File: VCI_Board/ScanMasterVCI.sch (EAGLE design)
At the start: 72 parts, among them IC1 XMEGA16A4A, IC2 CD4081B, IC8 SN74AHCT1G04, Q13 MMBT3904, Q14 MMBT3904, Q15 MMBT3904, Q16 MMBT3904, Q17 MMBT3904, Q2 MMBT4403, Q3 MMBT3904, Q4 MMBT4403, Q7 ZXMP6A17G, U1 MAX17502FATB+, U2 SN65HVDA195-Q1, U3 MAX17502EATB+

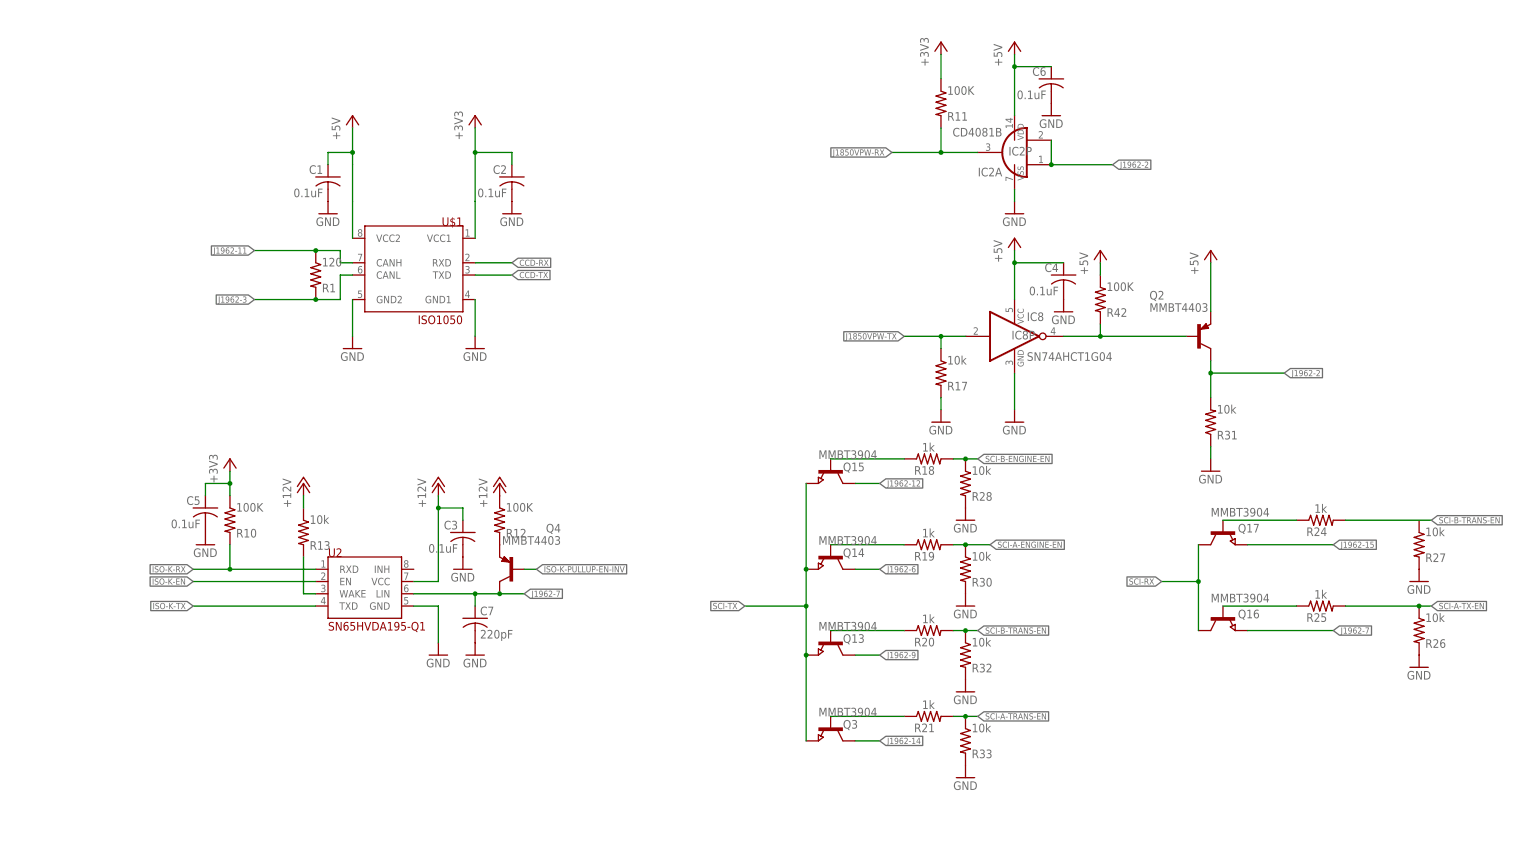
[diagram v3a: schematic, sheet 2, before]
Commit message: Re-wrote ISO9141 pull-up, J1850VPW circuit. ISO9141 pull-up resistor activation works on ISO-K-EN line now, removing the need for ISO-K-PULLUP-EN-INV line. However, it requires a double-transistor to work. J1850VPW circuit now works on +8V like it should, and the RX uses a simple voltage divider to judge the current state of J1850+. Credit goes to Konstantin for his suggestions on the circuits.
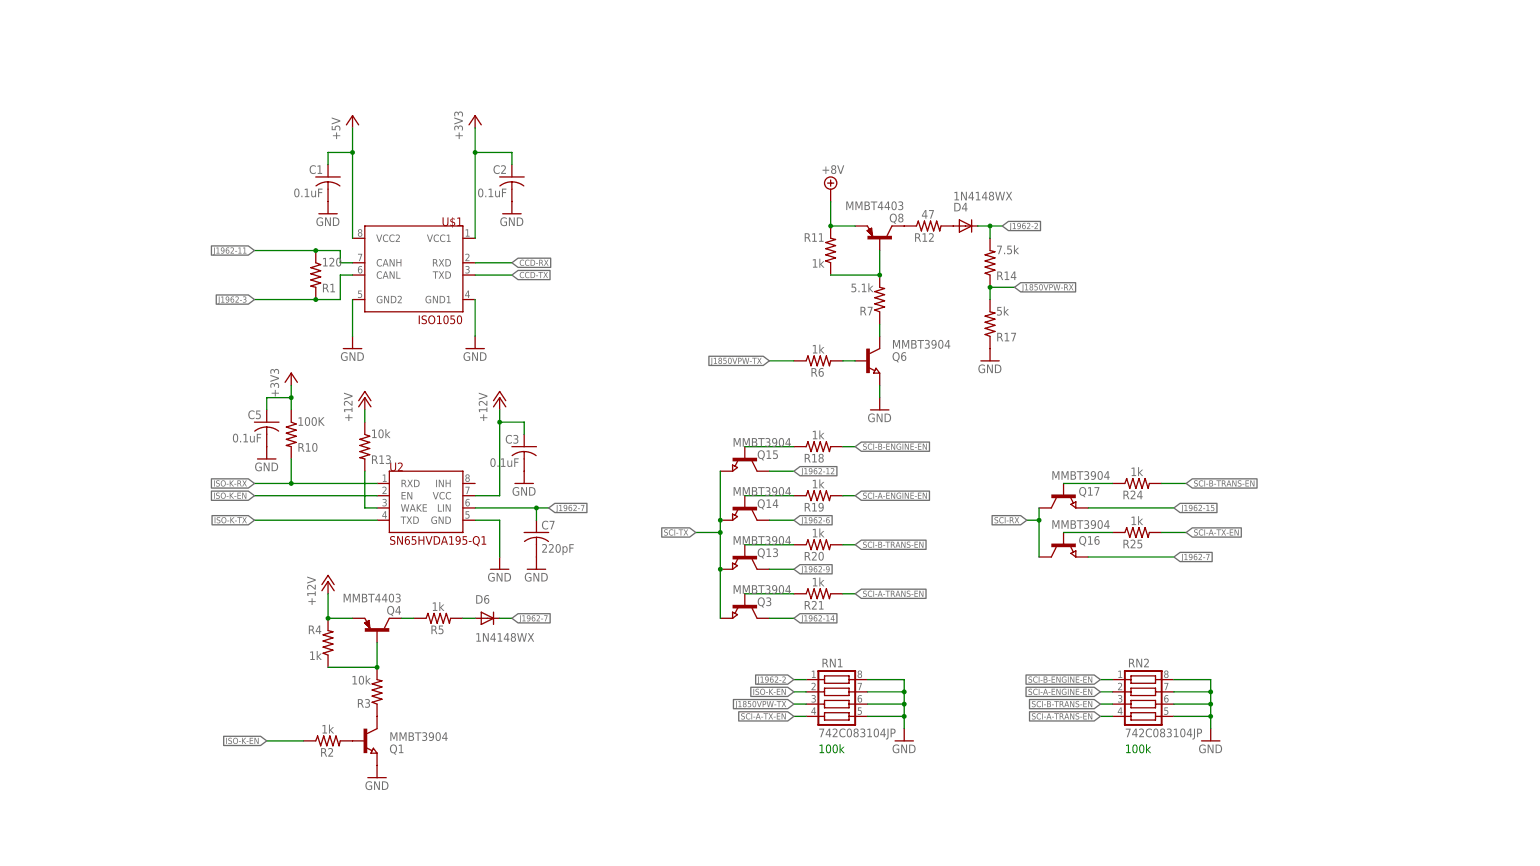
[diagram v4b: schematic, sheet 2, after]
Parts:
- removed C4, C6: 0.1uF, adafruit:C-USC0805
- removed IC2: CD4081B, 40xx:4081D
- removed IC8: SN74AHCT1G04, 74xx-little-us:74AHC1G04DBV
- removed Q2: MMBT4403, transistor-pnp:MMBT4403LT1SMD
- removed R26, R27, R28, R30, R32, R33: 10k, adafruit:R-US_R0805
- removed R31: 10k, adafruit:R-US_R0805W
- removed R42: 100K, adafruit:R-US_R0805W
- added D4, D6: 1N4148WX, diode:DIODE-SOD323-R
- added Q1, Q6: MMBT3904, semicon-smd-ipc:NPN-TRANSISTOR_SOT23
- added Q5: ZXTR2108FQ, customics:ZXTR2108FQ
- added Q8: MMBT4403, transistor-pnp:MMBT4403LT1SMD
- added R14: 7.5k, adafruit:R-US_R0805
- added R2, R4, R5, R6: 1k, adafruit:R-US_R0805
- added R3: 10k, adafruit:R-US_R0805
- added R7: 5.1k, adafruit:R-US_R0805
- added RN1, RN2: 742C083104JP, resistor-net:CTS742C083
- R11: value 100K -> 1k; device adafruit:R-US_R0805W -> adafruit:R-US_R0805
- R12: value 100K -> 47; device adafruit:R-US_R0805W -> adafruit:R-US_R0805
- R17: value 10k -> 5k
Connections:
- removed net ISO-K-PULLUP-EN-INV: IC1.PD4, Q4.B
- removed net J1962-5: J1962_1.5
- removed net N$1: U$1.VCC2
- removed net N$4: U$1.VCC1
- removed net N$5: IC8A.O, Q2.B, R42.2
- new net +8V: Q5.+8V, Q8.E, R11.2
- new net N$11: Q4.B, R3.2, R4.1
- new net N$26: Q6.C, R7.1
- new net N$27: Q4.C, R5.1
- new net N$28: Q8.B, R11.1, R7.2
- new net N$29: Q8.C, R12.1
- new net N$30: D4.A, R12.2
- new net N$31: D6.A, R5.2
- new net N$6: Q6.B, R6.2
- new net N$8: Q1.B, R2.2
- net +12V: now also Q4.E, Q5.VIN, R4.2; no longer R12.1
- net +3V3: now also U$1.VCC1; no longer R11.1
- net +5V: now also U$1.VCC2; no longer C4.1, C6.1, IC2P.VDD, IC8P.VCC, Q2.E, R42.1
- net GND: now also Q1.E, Q5.GND, Q6.E, R17.1, RN1.5, RN1.6, RN1.7, RN1.8, RN2.5, RN2.6, RN2.7, RN2.8; no longer C4.2, C6.2, IC2P.VSS, IC8P.GND, R17.2, R26.2, R27.2, R28.2, R30.2, R31.1, R32.2, R33.2
- net ISO-K-EN: now also R2.1, RN1.2
- net J1850VPW-RX: now also R14.1, R17.2; no longer IC2A.O, R11.2
- net J1850VPW-TX: now also R6.1, RN1.3; no longer IC8A.I, R17.1
- net J1962-2: now also D4.C, R14.2, RN1.1; no longer IC2A.I0, IC2A.I1, Q2.C, R31.2
- net J1962-7: now also D6.C; no longer Q4.C
- net N$10: now also Q1.C, R3.1; no longer Q4.E, R12.2
- net SCI-A-ENGINE-EN: now also RN2.2; no longer R30.1
- net SCI-A-TRANS-EN: now also RN2.4; no longer R33.1
- net SCI-A-TX-EN: now also RN1.4; no longer R26.1
- net SCI-B-ENGINE-EN: now also RN2.1; no longer R28.1
- net SCI-B-TRANS-EN: now also RN2.3; no longer R32.1
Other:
- note added: "100k"
- moved on the sheet: C3, C5, C7, Q13, Q14, Q15, Q16, Q17, Q3, Q4, R10, R11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

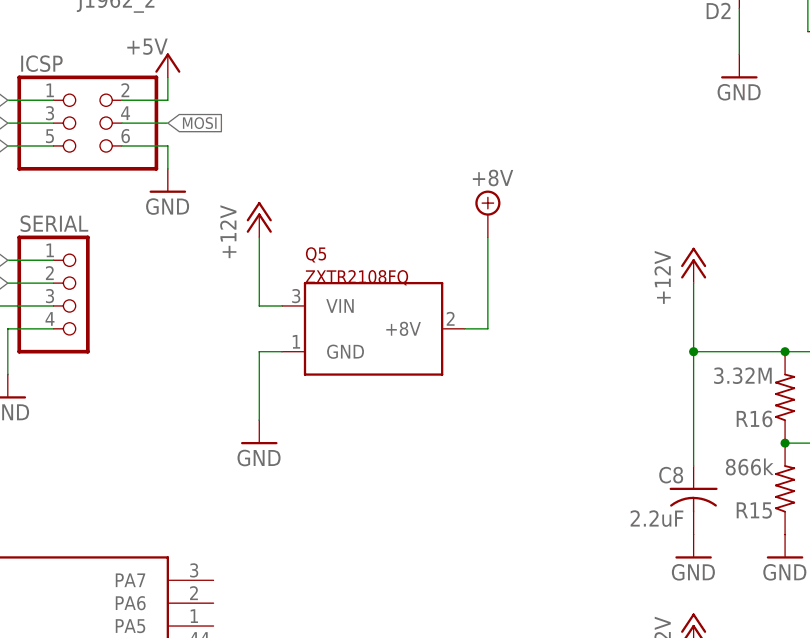
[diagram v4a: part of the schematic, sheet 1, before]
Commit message: Replaced J1850 8V supply IC with a beefier one. J1850VPW spec says max current is somewhere around 25 mA @ 8V, so I replaced the IC I was using with a beefier one. Less efficient, probably, but should be effective.
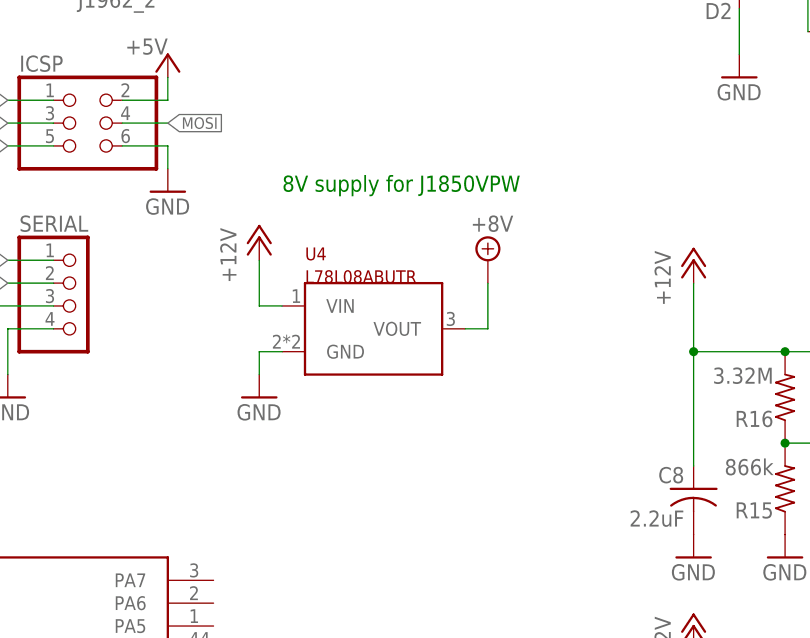
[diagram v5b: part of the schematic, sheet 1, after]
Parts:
- removed Q5: ZXTR2108FQ, customics:ZXTR2108FQ
- added U4: L78L08ABUTR, customics:L78L
- U1, U3: device customics:MAX17502EATB+ -> customics:MAX17502
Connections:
- net +12V: now also U4.VIN; no longer Q5.VIN
- net +8V: now also U4.VOUT; no longer Q5.+8V
- net GND: now also U4.GND; no longer Q5.GND
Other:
- note added: "8V supply for J1850VPW"
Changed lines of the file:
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@@
 <part name="GND2" library="supply1" library_urn="urn:adsk.eagle:library:371" deviceset="GND" device=""/>
 <part name="+3V1" library="supply1" library_urn="urn:adsk.eagle:library:371" deviceset="+3V3" device=""/>
-<part name="U3" library="customics" deviceset="MAX17502EATB+" device="" value="MAX17502EATB+"/>
 <part name="C9" library="adafruit" library_urn="urn:adsk.eagle:library:420" deviceset="C-US" device="C0805" value="3300pF"/>
 <part name="C11" library="adafruit" library_urn="urn:adsk.eagle:library:420" deviceset="C-US" device="C0805" value="2.2uF"/>
@@
 <part name="D1" library="diode" library_urn="urn:adsk.eagle:library:210" deviceset="ZENER-DIODE" device="SMB" package3d_urn="urn:adsk.eagle:package:43404/2" value="SMAJ5.0A"/>
 <part name="GND22" library="supply1" library_urn="urn:adsk.eagle:library:371" deviceset="GND" device=""/>
-<part name="U1" library="customics" deviceset="MAX17502EATB+" device="" value="MAX17502FATB+"/>
 <part name="D2" library="diode" library_urn="urn:adsk.eagle:library:210" deviceset="ZENER-DIODE" device="SMB" package3d_urn="urn:adsk.eagle:package:43404/2" value="1.5SMC43AT3G "/>
 <part name="GND33" library="supply1" library_urn="urn:adsk.eagle:library:371" deviceset="GND" device=""/>
@@
 <part name="P+3" library="supply1" library_urn="urn:adsk.eagle:library:371" deviceset="+12V" device=""/>
 <part name="R5" library="adafruit" library_urn="urn:adsk.eagle:library:420" deviceset="R-US_" device="R0805" value="1k"/>
-<part name="Q5" library="customics" deviceset="ZXTR2108FQ" device=""/>
 <part name="GND26" library="supply1" library_urn="urn:adsk.eagle:library:371" deviceset="GND" device=""/>
 <part name="P+4" library="supply1" library_urn="urn:adsk.eagle:library:371" deviceset="+12V" device=""/>
@@
 <part name="D4" library="diode" library_urn="urn:adsk.eagle:library:210" deviceset="DIODE-" device="SOD323-R" package3d_urn="urn:adsk.eagle:package:43437/1" value="1N4148WX"/>
 <part name="D6" library="diode" library_urn="urn:adsk.eagle:library:210" deviceset="DIODE-" device="SOD323-R" package3d_urn="urn:adsk.eagle:package:43437/1" value="1N4148WX"/>
+<part name="U4" library="customics" deviceset="L78L" device="" value="L78L08ABUTR"/>
+<part name="U3" library="customics" deviceset="MAX17502" device="" value="MAX17502EATB+"/>
+<part name="U1" library="customics" deviceset="MAX17502" device="" value="MAX17502FATB+"/>
 </parts>
 <sheets>
@@
 <text x="139.7" y="83.82" size="2.54" layer="91">Filtered Battery Volts -&gt; +3.3V</text>
 <text x="33.02" y="177.8" size="1.27" layer="91">SCI Engine</text>
+<text x="78.74" y="132.08" size="1.778" layer="91">8V supply for J1850VPW</text>
 </plain>
 <instances>
@@
 <instance part="GND2" gate="1" x="12.7" y="48.26"/>
 <instance part="+3V1" gate="G$1" x="12.7" y="68.58"/>
-<instance part="U3" gate="G$1" x="170.18" y="71.12"/>
 <instance part="C9" gate="G$1" x="182.88" y="58.42"/>
 <instance part="C11" gate="G$1" x="124.46" y="58.42" rot="MR0"/>
@@
 <instance part="D1" gate="G$1" x="223.52" y="106.68" rot="R90"/>
 <instance part="GND22" gate="1" x="223.52" y="91.44"/>
-<instance part="U1" gate="G$1" x="170.18" y="111.76"/>
 <instance part="D2" gate="G$1" x="129.54" y="154.94" smashed="yes" rot="R90">
 <attribute name="NAME" x="128.778" y="153.035" size="1.778" layer="95" rot="R180"/>
@@
 <instance part="GND16" gate="1" x="208.28" y="91.44"/>
 <instance part="GND19" gate="1" x="187.96" y="91.44"/>
-<instance part="Q5" gate="G$1" x="88.9" y="116.84"/>
-<instance part="GND26" gate="1" x="76.2" y="104.14"/>
-<instance part="P+4" gate="1" x="76.2" y="129.54"/>
-<instance part="SUPPLY1" gate="+8V" x="101.6" y="129.54"/>
+<instance part="GND26" gate="1" x="76.2" y="109.22"/>
+<instance part="P+4" gate="1" x="76.2" y="127"/>
+<instance part="SUPPLY1" gate="+8V" x="101.6" y="124.46"/>
+<instance part="U4" gate="G$1" x="88.9" y="116.84"/>
+<instance part="U3" gate="G$1" x="170.18" y="71.12"/>
+<instance part="U1" gate="G$1" x="170.18" y="111.76"/>
 </instances>
 <busses>
@@
 <wire x1="157.48" y1="76.2" x2="152.4" y2="76.2" width="0.1524" layer="91"/>
 <wire x1="152.4" y1="76.2" x2="152.4" y2="53.34" width="0.1524" layer="91"/>
+<pinref part="GND24" gate="1" pin="GND"/>
 <pinref part="U3" gate="G$1" pin="PGND"/>
-<pinref part="GND24" gate="1" pin="GND"/>
 </segment>
 <segment>
 <wire x1="182.88" y1="73.66" x2="198.12" y2="73.66" width="0.1524" layer="91"/>
-<pinref part="U3" gate="G$1" pin="GND"/>
 <wire x1="198.12" y1="73.66" x2="198.12" y2="53.34" width="0.1524" layer="91"/>
 <pinref part="GND27" gate="1" pin="GND"/>
+<pinref part="U3" gate="G$1" pin="GND"/>
 </segment>
 <segment>
@@
 </segment>
 <segment>
-<pinref part="Q5" gate="G$1" pin="GND"/>
 <wire x1="78.74" y1="114.3" x2="76.2" y2="114.3" width="0.1524" layer="91"/>
-<wire x1="76.2" y1="114.3" x2="76.2" y2="106.68" width="0.1524" layer="91"/>
+<wire x1="76.2" y1="114.3" x2="76.2" y2="111.76" width="0.1524" layer="91"/>
 <pinref part="GND26" gate="1" pin="GND"/>
+<pinref part="U4" gate="G$1" pin="GND"/>
 </segment>
 </net>
@@
 <wire x1="208.28" y1="60.96" x2="208.28" y2="78.74" width="0.1524" layer="91"/>
 <junction x="208.28" y="78.74"/>
-<pinref part="U3" gate="G$1" pin="FB_VO"/>
 <wire x1="157.48" y1="66.04" x2="154.94" y2="66.04" width="0.1524" layer="91"/>
 <wire x1="154.94" y1="66.04" x2="154.94" y2="60.96" width="0.1524" layer="91"/>
 <wire x1="208.28" y1="60.96" x2="154.94" y2="60.96" width="0.1524" layer="91"/>
 <junction x="208.28" y="60.96"/>
+<pinref part="U3" gate="G$1" pin="FB_VO"/>
 </segment>
 </net>
 <net name="N$9" class="0">
 <segment>
-<pinref part="U3" gate="G$1" pin="VCC"/>
 <wire x1="157.48" y1="68.58" x2="144.78" y2="68.58" width="0.1524" layer="91"/>
 <pinref part="C10" gate="G$1" pin="1"/>
 <wire x1="144.78" y1="68.58" x2="144.78" y2="60.96" width="0.1524" layer="91"/>
+<pinref part="U3" gate="G$1" pin="VCC"/>
 </segment>
 </net>
@@
 <pinref part="R8" gate="G$1" pin="2"/>
 <pinref part="R9" gate="G$1" pin="1"/>
-<pinref part="U3" gate="G$1" pin="EN_UVLO"/>
 <wire x1="157.48" y1="71.12" x2="139.7" y2="71.12" width="0.1524" layer="91"/>
 <wire x1="139.7" y1="71.12" x2="139.7" y2="63.5" width="0.1524" layer="91"/>
 <wire x1="139.7" y1="63.5" x2="134.62" y2="63.5" width="0.1524" layer="91"/>
 <junction x="134.62" y="63.5"/>
+<pinref part="U3" gate="G$1" pin="EN_UVLO"/>
 </segment>
 </net>
@@
 <wire x1="134.62" y1="73.66" x2="124.46" y2="73.66" width="0.1524" layer="91"/>
 <wire x1="124.46" y1="73.66" x2="124.46" y2="81.28" width="0.1524" layer="91"/>
-<pinref part="U3" gate="G$1" pin="VIN"/>
 <pinref part="R9" gate="G$1" pin="2"/>
 <junction x="134.62" y="73.66"/>
@@
 <wire x1="124.46" y1="60.96" x2="124.46" y2="73.66" width="0.1524" layer="91"/>
 <junction x="124.46" y="73.66"/>
+<pinref part="U3" gate="G$1" pin="VIN"/>
 </segment>
 <segment>
@@
 <wire x1="134.62" y1="114.3" x2="157.48" y2="114.3" width="0.1524" layer="91"/>
 <junction x="134.62" y="114.3"/>
-<pinref part="U1" gate="G$1" pin="VIN"/>
 <pinref part="C8" gate="G$1" pin="1"/>
 <wire x1="124.46" y1="101.6" x2="124.46" y2="114.3" width="0.1524" layer="91"/>
 <junction x="124.46" y="114.3"/>
+<pinref part="U1" gate="G$1" pin="VIN"/>
 </segment>
 <segment>
@@
 </segment>
 <segment>
-<pinref part="Q5" gate="G$1" pin="VIN"/>
 <wire x1="78.74" y1="119.38" x2="76.2" y2="119.38" width="0.1524" layer="91"/>
-<wire x1="76.2" y1="119.38" x2="76.2" y2="127" width="0.1524" layer="91"/>
+<wire x1="76.2" y1="119.38" x2="76.2" y2="124.46" width="0.1524" layer="91"/>
 <pinref part="P+4" gate="1" pin="+12V"/>
+<pinref part="U4" gate="G$1" pin="VIN"/>
 </segment>
 </net>
@@
 <wire x1="195.58" y1="78.74" x2="187.96" y2="78.74" width="0.1524" layer="91"/>
 <wire x1="187.96" y1="78.74" x2="187.96" y2="76.2" width="0.1524" layer="91"/>
+<wire x1="187.96" y1="76.2" x2="182.88" y2="76.2" width="0.1524" layer="91"/>
 <pinref part="U3" gate="G$1" pin="LX"/>
-<wire x1="187.96" y1="76.2" x2="182.88" y2="76.2" width="0.1524" layer="91"/>
 </segment>
 </net>
@@
 <segment>
 <wire x1="144.78" y1="109.22" x2="157.48" y2="109.22" width="0.1524" layer="91"/>
-<pinref part="U1" gate="G$1" pin="VCC"/>
 <pinref part="C13" gate="G$1" pin="1"/>
 <wire x1="144.78" y1="101.6" x2="144.78" y2="109.22" width="0.1524" layer="91"/>
+<pinref part="U1" gate="G$1" pin="VCC"/>
 </segment>
 </net>
@@
 <segment>
 <wire x1="187.96" y1="106.68" x2="182.88" y2="106.68" width="0.1524" layer="91"/>
-<pinref part="U1" gate="G$1" pin="SS"/>
 <pinref part="C14" gate="G$1" pin="1"/>
 <wire x1="187.96" y1="101.6" x2="187.96" y2="106.68" width="0.1524" layer="91"/>
+<pinref part="U1" gate="G$1" pin="SS"/>
 </segment>
 </net>
@@
 <junction x="208.28" y="101.6"/>
 <junction x="208.28" y="119.38"/>
-<pinref part="U1" gate="G$1" pin="FB_VO"/>
 <wire x1="154.94" y1="106.68" x2="157.48" y2="106.68" width="0.1524" layer="91"/>
 <wire x1="154.94" y1="106.68" x2="154.94" y2="101.6" width="0.1524" layer="91"/>
 <wire x1="208.28" y1="101.6" x2="154.94" y2="101.6" width="0.1524" layer="91"/>
+<pinref part="U1" gate="G$1" pin="FB_VO"/>
 </segment>
 </net>
@@
 <segment>
 <pinref part="C9" gate="G$1" pin="1"/>
+<wire x1="182.88" y1="60.96" x2="182.88" y2="66.04" width="0.1524" layer="91"/>
 <pinref part="U3" gate="G$1" pin="SS"/>
-<wire x1="182.88" y1="60.96" x2="182.88" y2="66.04" width="0.1524" layer="91"/>
 </segment>
 </net>
 <net name="+8V" class="0">
 <segment>
-<pinref part="Q5" gate="G$1" pin="+8V"/>
 <wire x1="99.06" y1="116.84" x2="101.6" y2="116.84" width="0.1524" layer="91"/>
-<wire x1="101.6" y1="116.84" x2="101.6" y2="127" width="0.1524" layer="91"/>
+<wire x1="101.6" y1="116.84" x2="101.6" y2="121.92" width="0.1524" layer="91"/>
 <pinref part="SUPPLY1" gate="+8V" pin="+8V"/>
-</segment>
-</net>
+<pinref part="U4" gate="G$1" pin="VOUT"/>
+</segment>
+</net>
